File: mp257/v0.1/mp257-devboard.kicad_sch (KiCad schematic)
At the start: 39 parts, among them CON1 microSDCon_SMT_104031-0811, J1 Pins_02x40_P0.4mm_W3.0mm_SMT, J2 Pins_02x40_P0.4mm_W3.0mm_SMT, J3 USB-C_Receptacle_Molex_217179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, J4 Pins_02x04_RightAngle_P2.54mm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, J5 Conn_01x02, J6 Pins_02x05_P1.27mm_SMT, U1 STM32MP257FAK3, U3 USBLC6-2SC6, U5 NORFLASH_W25Q128JV, X1 XTAL_4_PINS

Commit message: Fix ref nums pasted from reference schematic
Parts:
- renumbered C4 to C90, C3 to C92, X1 to X2
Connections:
- net GND: now also S3.1; no longer R72.2
- net VDD: now also R72.2; no longer S3.1
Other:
- sheet Power ports: added WAKEUP_BUT; removed none
- note added: "NOR Flash"
- moved on the sheet: BOOT0_2, C21, J1, J2, J3, J5, R10, R11, R3, R4, R5, R6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

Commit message: Fix all refs: no duplicates
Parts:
- renumbered C12 to C120, C21 to C210, R11 to R12, R2 to R9
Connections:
- no-connect marks 198 -> 199
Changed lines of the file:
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@@
 	)
 	(no_connect
+		(at 189.23 481.33)
+	)
+	(no_connect
 		(at 346.71 518.16)
 	)
@@
 		(dnp no)
 		(fields_autoplaced yes)
-		(property "Reference" "R2"
+		(property "Reference" "R9"
 			(at 175.26 275.5899 0)
 			(effects
@@
 			(project "mp153-devboard"
 				(path "/64ec1a6b-f4f9-4414-abbd-a05816451f08"
-					(reference "R2")
+					(reference "R9")
 					(unit 1)
 				)
@@
 		(dnp no)
 		(fields_autoplaced yes)
-		(property "Reference" "C21"
+		(property "Reference" "C210"
 			(at 231.14 202.5586 0)
 			(effects
@@
 			(project "Kit-Brainboard"
 				(path "/64ec1a6b-f4f9-4414-abbd-a05816451f08"
-					(reference "C21")
+					(reference "C210")
 					(unit 1)
 				)
@@
 		(dnp no)
 		(fields_autoplaced yes)
-		(property "Reference" "R11"
+		(property "Reference" "R12"
 			(at 279.4 88.8999 0)
 			(effects
@@
 			(project "mp153-devboard"
 				(path "/64ec1a6b-f4f9-4414-abbd-a05816451f08"
-					(reference "R11")
+					(reference "R12")
 					(unit 1)
 				)
@@
 		(dnp no)
 		(fields_autoplaced yes)
-		(property "Reference" "C12"
-			(at 102.87 268.6113 0)
+		(property "Reference" "C120"
+			(at 102.87 267.9762 0)
 			(effects
 				(font
@@
 		)
 		(property "Display" "0.1uF"
-			(at 102.87 271.1513 0)
+			(at 102.87 270.5162 0)
 			(effects
 				(font
@@
 			(project "Kit-Brainboard"
 				(path "/64ec1a6b-f4f9-4414-abbd-a05816451f08"
-					(reference "C12")
+					(reference "C120")
 					(unit 1)
 				)

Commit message: WIP: symbols
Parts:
- U1: symbol MCD_PARTS_database:U_STM32MP25XXAK I_Os_0_STM32MP257FAK3_MCD_PARTS_database.DbLib -> 4ms_IC:STM32MP257FAKx
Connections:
- net VDDA1V8_AON is gone; now on net VDDA_1V8: U1.W2 (PDR_ON)
- net PC10: no longer CON1.1 (DAT2), J1.13 (Pin_13), J1.14 (Pin_14)
- net PC11: no longer CON1.2 (CD/DAT3), J1.15 (Pin_15), J1.16 (Pin_16)
- net PC12: no longer CON1.5 (CLK), J1.19 (Pin_19), J1.20 (Pin_20)
- net PC8: no longer CON1.7 (DAT0), J1.7 (Pin_7), J1.8 (Pin_8), R1.2
- net PC9: no longer CON1.8 (DAT1), J1.10 (Pin_10), J1.9 (Pin_9)
- net PD2: no longer CON1.3 (CMD), J1.17 (Pin_17), J1.18 (Pin_18), R9.2
- net VDDIO renamed VDD_IO
- net eMMC.SDMMC2_CK: no longer names the net of U1.B25 (PE14)
- net eMMC.SDMMC2_CMD: no longer names the net of U1.D24 (PE15)
- net eMMC.SDMMC2_D0: no longer names the net of U1.C24 (PE13)
- net eMMC.SDMMC2_D1: no longer names the net of U1.B23 (PE11)
- net eMMC.SDMMC2_D2: no longer names the net of U1.C23 (PE8)
- net eMMC.SDMMC2_D3: no longer names the net of U1.C25 (PE12)
- net eMMC.SDMMC2_D4: no longer names the net of U1.D22 (PE10)
- net eMMC.SDMMC2_D5: no longer names the net of U1.A23 (PE9)
- net eMMC.SDMMC2_D6: no longer names the net of U1.A22 (PE6)
- net eMMC.SDMMC2_D7: no longer names the net of U1.B22 (PE7)
- new net SDMMC_CLK: CON1.5 (CLK), J1.19 (Pin_19), J1.20 (Pin_20)
- new net SDMMC_CMD: CON1.3 (CMD), J1.17 (Pin_17), J1.18 (Pin_18), R9.2
- new net SDMMC_D0: CON1.7 (DAT0), J1.7 (Pin_7), J1.8 (Pin_8), R1.2
- new net SDMMC_D1: CON1.8 (DAT1), J1.10 (Pin_10), J1.9 (Pin_9)
- new net SDMMC_D2: CON1.1 (DAT2), J1.13 (Pin_13), J1.14 (Pin_14)
- new net SDMMC_D3: CON1.2 (CD/DAT3), J1.15 (Pin_15), J1.16 (Pin_16)
- no-connect marks 199 -> 209
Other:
- note removed: "PMIC"

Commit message: Updated RAM and STM32MP2 footprints to 4ms lib
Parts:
- U1: footprint ICC_TFBGA424_14X14_P050_H1P20_CODE-B0A2 -> 4ms_Package_QFP:TFBGA-424_14x14mm_P0.5_STM_AK

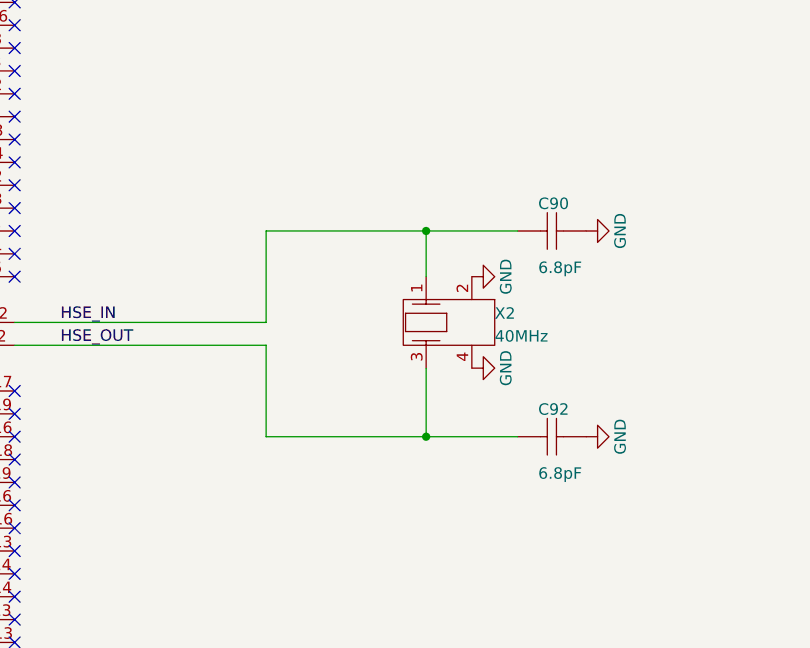
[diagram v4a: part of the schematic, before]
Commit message: Updating parts to 4ms lib
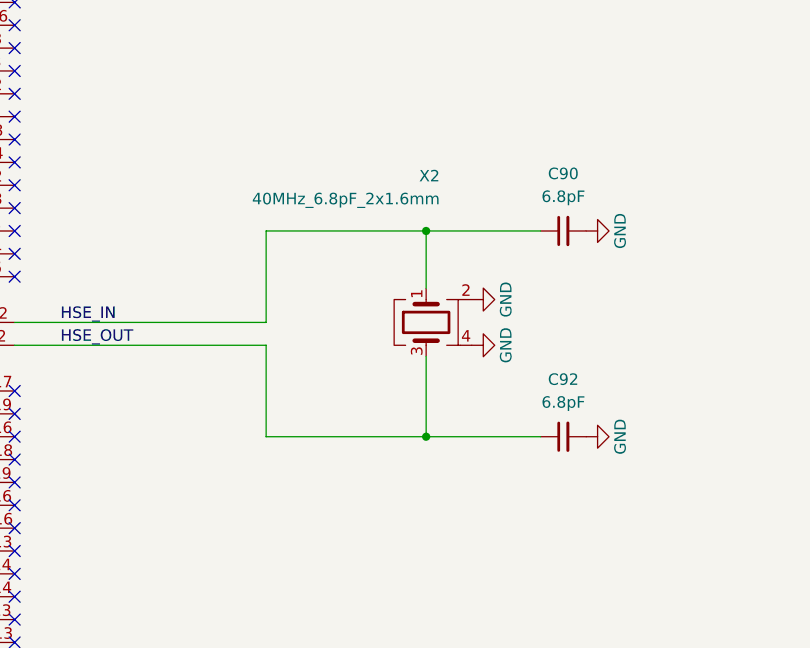
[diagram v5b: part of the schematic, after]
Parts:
- C90: value Capacitor -> 6.8pF_0402_25V; footprint C0402 -> 4ms_Capacitor:C_0402; symbol MCD_PARTS_database:U_STM32MP25XXAK I_Os_0_mirrored_Capacitor_MCD_PARTS_database.DbLib -> 4ms_Capacitor:6.8pF_0402_25V; ALTERNATE_MANUFACTURER N/A -> (none); ALTERNATE_MANUFACTURER_PART_NUMBER N/A -> (none); ALTIUM_VALUE 6.8pF -> (none); COMPONENTLINK1DESCRIPTION Datasheet -> (none); COMPONENTLINK1URL http://tunmcdsvn.tun.st.com/Component_Documentation_Library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 -> (none); COMPONENT_COUNTRY_OF_ORIGIN China -> (none); Display (none) -> 6.8pF; ECCN_EU n/a -> (none); ECCN_US n/a -> (none); ID 3068 -> (none); INITIAL_BOARD_REFERENCE MB1319 -> (none); INTERNAL_PART_NUMBER MCD-00674 -> (none); JLCPCB ID (none) -> C1576; MANUFACTURER YAGEO -> (none); MANUFACTURER_PART_NUMBER CC0402CRNPO9BN6R8 -> (none); Manufacturer (none) -> Yageo; ORDER_CODE_DIGIKEY 311-3327-1-ND -> (none); ORDER_CODE_FARNELL N/A -> (none); ORDER_CODE_RS N/A -> (none); PACKAGE 0402 -> (none); PART_PREFERENCE Recommended -> (none); PART_TYPE Capacitor -> (none); PROVIDED_BY SUBCO -> (none); Part Number (none) -> CC0402CRNPO9BN6R8; Production Stage (none) -> A; SHOWFIELDS YES -> (none); STATUS Released -> (none); Specifications (none) -> 6.8pF, Min. 25V 10%, NP0/C0G
- C92: value Capacitor -> 6.8pF_0402_25V; footprint C0402 -> 4ms_Capacitor:C_0402; symbol MCD_PARTS_database:U_STM32MP25XXAK I_Os_2_mirrored_Capacitor_MCD_PARTS_database.DbLib -> 4ms_Capacitor:6.8pF_0402_25V; ALTERNATE_MANUFACTURER N/A -> (none); ALTERNATE_MANUFACTURER_PART_NUMBER N/A -> (none); ALTIUM_VALUE 6.8pF -> (none); COMPONENTLINK1DESCRIPTION Datasheet -> (none); COMPONENTLINK1URL http://tunmcdsvn.tun.st.com/Component_Documentation_Library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 -> (none); COMPONENT_COUNTRY_OF_ORIGIN China -> (none); Display (none) -> 6.8pF; ECCN_EU n/a -> (none); ECCN_US n/a -> (none); ID 3068 -> (none); INITIAL_BOARD_REFERENCE MB1319 -> (none); INTERNAL_PART_NUMBER MCD-00674 -> (none); JLCPCB ID (none) -> C1576; MANUFACTURER YAGEO -> (none); MANUFACTURER_PART_NUMBER CC0402CRNPO9BN6R8 -> (none); Manufacturer (none) -> Yageo; ORDER_CODE_DIGIKEY 311-3327-1-ND -> (none); ORDER_CODE_FARNELL N/A -> (none); ORDER_CODE_RS N/A -> (none); PACKAGE 0402 -> (none); PART_PREFERENCE Recommended -> (none); PART_TYPE Capacitor -> (none); PROVIDED_BY SUBCO -> (none); Part Number (none) -> CC0402CRNPO9BN6R8; Production Stage (none) -> A; SHOWFIELDS YES -> (none); STATUS Released -> (none); Specifications (none) -> 6.8pF, Min. 25V 10%, NP0/C0G
- X2: value XTAL_4_PINS -> 40MHz_6.8pF_2x1.6mm; footprint CRY_NX1612SA_4P -> 4ms_Crystal:Crystal_2.0x1.6mm_4pin; symbol MCD_PARTS_database:U_STM32MP25XXAK I_Os_0_XTAL_4_PINS_MCD_PARTS_database.DbLib -> 4ms_Crystal:40MHz_6.8pF_2x1.6mm; ALTIUM_VALUE 40MHz -> (none); COMPONENTLINK1URL http://tunmcdsvn.tun.st.com/Component_Documentation_Library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 -> (none); COMPONENT_COUNTRY_OF_ORIGIN Unknown -> (none); ID 4450 -> (none); INTERNAL_PART_NUMBER MCD-02344 -> (none); MANUFACTURER NDK -> (none); MANUFACTURER_PART_NUMBER NX1612SA-40MHZ-EXS00A-CS13836 -> (none); Manufacturer (none) -> ECS; ORDER_CODE_DIGIKEY N/A -> (none); ORDER_CODE_FARNELL N/A -> (none); ORDER_CODE_RS N/A -> (none); PACKAGE 1.6x1.2mm -> (none); PART_PREFERENCE Recommended -> (none); PART_TYPE Crystal_Osc -> (none); Production Stage (none) -> A; SHOWFIELDS YES -> (none); STATUS Checked -> (none); Specifications (none) -> 40MHz 6.8pF Crystal Resonator, 10ppm, 2016 2x1.6mm
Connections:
- net GND: now also C90.2; no longer C90.1
- net HSE_IN: now also C90.1; no longer C90.2
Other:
- moved on the sheet: X2

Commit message: WIP
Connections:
- net NRSTC1MS: now also R272.1; no longer R272.2
- net PWR_CPU_ON: now also R272.2; no longer R272.1
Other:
- moved on the sheet: R272
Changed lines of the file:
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@@
 	(symbol
 		(lib_id "4ms_Resistor_0402:10k_0402")
-		(at 153.67 485.14 0)
+		(at 153.67 485.14 180)
 		(unit 1)
 		(exclude_from_sim no)
@@
 		(on_board yes)
 		(dnp no)
+		(fields_autoplaced yes)
 		(property "Reference" "R272"
-			(at 156.972 482.346 0)
+			(at 156.21 483.8699 0)
 			(effects
 				(font
 					(size 1.27 1.27)
 				)
-				(justify left bottom)
+				(justify right)
 			)
 		)
 		(property "Value" "10k_0402"
-			(at 151.13 485.14 90)
+			(at 156.21 485.14 90)
 			(effects
 				(font
@@
 		)
 		(property "Footprint" "4ms_Resistor:R_0402"
-			(at 151.13 498.094 0)
+			(at 156.21 472.186 0)
 			(effects
 				(font
@@
 		)
 		(property "Specifications" "10k, 1%, 1/16W, 0402"
-			(at 151.13 492.76 0)
+			(at 156.21 477.52 0)
 			(effects
 				(font
@@
 		)
 		(property "Manufacturer" "Yageo"
-			(at 151.13 494.538 0)
+			(at 156.21 475.742 0)
 			(effects
 				(font
@@
 		)
 		(property "Part Number" "RC0402FR-0710KL"
-			(at 151.13 496.316 0)
+			(at 156.21 473.964 0)
 			(effects
 				(font
@@
 		)
 		(property "Display" "10k"
-			(at 157.48 485.14 90)
+			(at 156.21 486.4099 0)
 			(effects
 				(font
 					(size 1.27 1.27)
 				)
+				(justify right)
 			)
 		)
 		(property "JLCPCB ID" "C60490"
-			(at 151.13 499.872 0)
+			(at 156.21 470.408 0)
 			(effects
 				(font
@@
 		)
 		(property "Production Stage" "A"
-			(at 151.13 501.65 0)
+			(at 156.21 468.63 0)
 			(effects
 				(font

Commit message: mp257 placement WIP
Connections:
- net PA0: no longer J2.31 (Pin_31), J2.32 (Pin_32)
- net PA1: no longer J2.33 (Pin_33), J2.34 (Pin_34)
- net PA2: no longer J2.35 (Pin_35), J2.36 (Pin_36)
- net PA3: no longer J2.53 (Pin_53), J2.54 (Pin_54)
- net PA4: no longer J2.41 (Pin_41), J2.42 (Pin_42)
- net PA5: no longer J2.37 (Pin_37), J2.38 (Pin_38)
- net PA6: no longer J2.57 (Pin_57), J2.58 (Pin_58)
- net PA7: no longer J2.29 (Pin_29), J2.30 (Pin_30)
- net PB1: no longer J2.47 (Pin_47), J2.48 (Pin_48)
- net PC1: no longer J2.49 (Pin_49), J2.50 (Pin_50)
- net PC2: no longer J2.61 (Pin_61), J2.62 (Pin_62)
- net PC3: no longer J2.55 (Pin_55), J2.56 (Pin_56)
- net PC4: no longer J2.43 (Pin_43), J2.44 (Pin_44)
- net PC5: no longer J2.45 (Pin_45), J2.46 (Pin_46)
- net PF11: no longer J2.39 (Pin_39), J2.40 (Pin_40)
- net PF12: no longer J2.59 (Pin_59), J2.60 (Pin_60)
- net PG13: no longer J2.51 (Pin_51), J2.52 (Pin_52)
- net ADC3_CH4: now reaches U1.AA13 (PH9)
- net ADC1_CH11: now reaches U1.AA15 (PF0)
- net ADC1_CH11: now also J2.55 (Pin_55), J2.56 (Pin_56)
- net ADC1_CH3: now reaches U1.AA7 (PG3)
- net ADC1_CH13: now reaches U1.AC15 (PF2)
- net ADC1_CH6: now reaches U1.AD4 (PG1)
- net ADC1_CH4: now reaches U1.AD6 (PG4)
- net ADC3_CH6: now reaches U1.AE4 (PF11)
- net ADC3_CH2: now reaches U1.AE5 (PF10)
- net ADC1_CH16: now reaches U1.AF11 (PF3)
- net ADC3_CH8: now reaches U1.AF14 (PH10)
- net ADC1_CH2: now reaches U1.AG5 (PG2)
- net ADC1_CH12: now reaches U1.AA9 (PC3)
- net ADC1_CH12: now also J2.59 (Pin_59), J2.60 (Pin_60)
- net ADC1_CH9: now reaches U1.AB10 (PC6)
- net ADC1_CH10: now reaches U1.AD10 (PC5)
- net ADC1_CH7: now reaches U1.AD8 (PC11)
- net ADC1_CH15: now reaches U1.AE6 (PB15)
- net ADC1_CH17: now reaches U1.AE7 (PC12)
- net ADC1_CH8: now reaches U1.AE9 (PC9)
- net ADC1_CH8: now also J2.57 (Pin_57), J2.58 (Pin_58)
- net ADC3_CH9: now reaches U1.AF9 (PC7)
- net ADC1_CH5: now reaches U1.AG10 (PC10)
- net ADC1_CH5: now also J2.53 (Pin_53), J2.54 (Pin_54)
- new net: J2.29 (Pin_29), J2.30 (Pin_30)
- new net: J2.31 (Pin_31), J2.32 (Pin_32)
- new net: J2.33 (Pin_33), J2.34 (Pin_34)
- new net: J2.35 (Pin_35), J2.36 (Pin_36)
- new net: J2.37 (Pin_37), J2.38 (Pin_38)
- new net: J2.39 (Pin_39), J2.40 (Pin_40)
- new net: J2.41 (Pin_41), J2.42 (Pin_42)
- new net: J2.43 (Pin_43), J2.44 (Pin_44)
- new net: J2.45 (Pin_45), J2.46 (Pin_46)
- new net: J2.47 (Pin_47), J2.48 (Pin_48)
- new net: J2.49 (Pin_49), J2.50 (Pin_50)
- new net: J2.51 (Pin_51), J2.52 (Pin_52)
- new net: J2.61 (Pin_61), J2.62 (Pin_62)
- no-connect marks 209 -> 89
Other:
- note added: "SPI-MISO"
- note added: "SPI-MOSI"
- note added: "SPI-NSS"
- note added: "SPI-SCK"
- note added: "SPI3"
- note added: "SPI5"
- note removed: "ADC2-6"
- note removed: "SPI1-MISO"
- note removed: "SPI1-MOSI"
- note removed: "SPI1-NSS"
- note removed: "SPI1-SCK"

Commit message: Routing SDMMC, SAI, I2C, ADCs
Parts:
- added J7: Conn_02x15_Odd_Even, 4ms_Connector:Connector-30pin-P0.4mm-W3.0mm, symbol Connector_Generic:Conn_02x15_Odd_Even
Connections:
- net ADC1_CH3: now also J2.17 (Pin_17), J2.18 (Pin_18)
- net ADC1_CH6: now also J2.37 (Pin_37), J2.38 (Pin_38)
- net ADC1_CH9: now also J2.73 (Pin_73), J2.74 (Pin_74)
- net ADC3_CH8: now also J2.61 (Pin_61), J2.62 (Pin_62)
- net BOOT0: now also U1.Y3 (BOOT0)
- net BOOT2: now also U1.AB1 (BOOT2)
- net GND: now also J7.1 (Pin_1), J7.3 (Pin_3), J7.5 (Pin_5), J7.7 (Pin_7), J7.9 (Pin_9)
- net PA10: no longer J1.63 (Pin_63), J1.64 (Pin_64)
- net PA11: no longer J1.55 (Pin_55), J1.56 (Pin_56)
- net PA5: now also J2.75 (Pin_75), J2.76 (Pin_76), U1.AE17 (PA5)
- net PA9: now also J2.71 (Pin_71), J2.72 (Pin_72), U1.AF15 (PA9); no longer J2.5 (Pin_5), J2.6 (Pin_6)
- net PB14: no longer J1.39 (Pin_39), J1.40 (Pin_40)
- net PB15: no longer J1.5 (Pin_5), J1.6 (Pin_6)
- net PB4: no longer J1.1 (Pin_1), J1.2 (Pin_2)
- net PB6: now also J1.3 (Pin_3), J1.4 (Pin_4), U1.C13 (PB6); no longer J2.13 (Pin_13), J2.14 (Pin_14)
- net PB8: no longer J1.3 (Pin_3), J1.4 (Pin_4)
- net PB9: no longer CON1.10 (SDDET1), J1.11 (Pin_11), J1.12 (Pin_12)
- net PD0: no longer J1.43 (Pin_43), J1.44 (Pin_44)
- net PD12: no longer J1.61 (Pin_61), J1.62 (Pin_62)
- net PD14: no longer J2.3 (Pin_3), J2.4 (Pin_4)
- net PD3: no longer J1.41 (Pin_41), J1.42 (Pin_42)
- net PD6: no longer J1.49 (Pin_49), J1.50 (Pin_50)
- net PD7: no longer J2.71 (Pin_71), J2.72 (Pin_72)
- net PE11: no longer J1.45 (Pin_45), J1.46 (Pin_46)
- net PE12: no longer J2.1 (Pin_1), J2.2 (Pin_2)
- net PE13: no longer J2.17 (Pin_17), J2.18 (Pin_18)
- net PE5: no longer J1.57 (Pin_57), J1.58 (Pin_58)
- net PE8: no longer J1.59 (Pin_59), J1.60 (Pin_60)
- net PF1: no longer J2.15 (Pin_15), J2.16 (Pin_16)
- net PF3: no longer J2.11 (Pin_11), J2.12 (Pin_12)
- net PG10: no longer J1.51 (Pin_51), J1.52 (Pin_52)
- net PG12: no longer J2.75 (Pin_75), J2.76 (Pin_76)
- net PG2: no longer J2.69 (Pin_69), J2.70 (Pin_70)
- net PG7: no longer J2.21 (Pin_21), J2.22 (Pin_22)
- net PH12: no longer J1.47 (Pin_47), J1.48 (Pin_48)
- net PH13: no longer J2.19 (Pin_19), J2.20 (Pin_20)
- net PH14: no longer J2.7 (Pin_7), J2.8 (Pin_8)
- net PH3: no longer J2.73 (Pin_73), J2.74 (Pin_74)
- net PH8: no longer J2.10 (Pin_10), J2.9 (Pin_9)
- net SDMMC_CLK: now also U1.C21 (PE3)
- net SDMMC_CMD: now also U1.C20 (PE2)
- net SDMMC_D0: now also U1.B21 (PE4)
- net SDMMC_D1: now also U1.C22 (PE5)
- net SDMMC_D2: now also U1.B19 (PE0)
- net SDMMC_D3: now also U1.C19 (PE1)
- net LTDC_VSYNC: now reaches U1.J3 (PI6)
- net LTDC_VSYNC: now also J7.2 (Pin_2)
- net LTDC_HSYNC: now reaches U1.J5 (PI7)
- net LTDC_HSYNC: now also J7.12 (Pin_12)
- net LTDC_DE: now reaches U1.K4 (PI5)
- net LTDC_DE: now also J7.4 (Pin_4)
- net LTDC_B3: now reaches U1.L7 (PI0)
- net LTDC_B3: now also J7.23 (Pin_23)
- net LTDC_B4: now reaches U1.M6 (PI1)
- net LTDC_B4: now also J7.21 (Pin_21)
- net LTDC_B5: now reaches U1.N5 (PI2)
- net LTDC_B5: now also J7.10 (Pin_10)
- net LTDC_B6: now reaches U1.N7 (PI3)
- net LTDC_B6: now also J7.8 (Pin_8)
- net LTDC_B7: now reaches U1.P6 (PI4)
- net LTDC_B7: now also J7.6 (Pin_6)
- net PE9: now reaches U1.A23 (PE9)
- net PE9: now also J1.41 (Pin_41), J1.42 (Pin_42)
- net PH7: now reaches U1.AE16 (PH7)
- net PH7: now also J2.5 (Pin_5), J2.6 (Pin_6)
- net PF9: now reaches U1.AE8 (PF9)
- net PF9: now also J2.1 (Pin_1), J2.2 (Pin_2)
- net SAI1_FS: now reaches U1.B23 (PE11)
- net SAI1_FS: now also J1.45 (Pin_45), J1.46 (Pin_46)
- net SAI1_MCLK: now reaches U1.B25 (PE14)
- net SAI1_MCLK: now also J1.43 (Pin_43), J1.44 (Pin_44)
- net SAI1_SD_A: now reaches U1.C24 (PE13)
- net SAI1_SD_A: now also J1.49 (Pin_49), J1.50 (Pin_50)
- net SAI1_SCK: now reaches U1.D24 (PE15)
- net SAI1_SCK: now also J1.47 (Pin_47), J1.48 (Pin_48)
- net LTDC_G2: now reaches U1.L5 (PG8)
- net LTDC_G2: now also J7.20 (Pin_20)
- net LTDC_G3: now reaches U1.M3 (PG9)
- net LTDC_G3: now also J7.22 (Pin_22)
- net LTDC_G4: now reaches U1.M4 (PG10)
- net LTDC_G4: now also J7.24 (Pin_24)
- net LTDC_G5: now reaches U1.N2 (PG11)
- net LTDC_G5: now also J7.26 (Pin_26)
- net LTDC_G6: now reaches U1.N3 (PG12)
- net LTDC_G6: now also J7.28 (Pin_28)
- net LTDC_G7: now reaches U1.P1 (PG13)
- net LTDC_G7: now also J7.30 (Pin_30)
- net LTDC_R3: now reaches U1.P3 (PF14)
- net LTDC_R3: now also J7.27 (Pin_27)
- net LTDC_CLK: now reaches U1.P4 (PF12)
- net LTDC_CLK: now also J7.25 (Pin_25)
- net LTDC_R4: now reaches U1.R2 (PF15)
- net LTDC_R4: now also J7.29 (Pin_29)
- net LTDC_R5: now reaches U1.R3 (PG5)
- net LTDC_R5: now also J7.14 (Pin_14)
- net LTDC_R6: now reaches U1.T3 (PG6)
- net LTDC_R6: now also J7.16 (Pin_16)
- net LTDC_R7: now reaches U1.U2 (PG7)
- net LTDC_R7: now also J7.18 (Pin_18)
- net I2C4_SCL: now reaches U1.A15 (PD11)
- net I2C4_SCL: now also J1.61 (Pin_61), J1.62 (Pin_62)
- net SAI1_SD_B: now reaches U1.A26 (PB13)
- net SAI1_SD_B: now also J1.51 (Pin_51), J1.52 (Pin_52)
- net I2C4_SDA: now reaches U1.C17 (PD10)
- net I2C4_SDA: now also J1.59 (Pin_59), J1.60 (Pin_60)
- new net: J2.10 (Pin_10), J2.9 (Pin_9)
- new net: J2.11 (Pin_11), J2.12 (Pin_12)
- new net: J2.13 (Pin_13), J2.14 (Pin_14)
- new net: J2.15 (Pin_15), J2.16 (Pin_16)
- new net: J2.19 (Pin_19), J2.20 (Pin_20)
- new net: J2.21 (Pin_21), J2.22 (Pin_22)
- new net: J2.3 (Pin_3), J2.4 (Pin_4)
- new net: J2.69 (Pin_69), J2.70 (Pin_70)
- new net: J2.7 (Pin_7), J2.8 (Pin_8)
- new net: J1.1 (Pin_1), J1.2 (Pin_2)
- new net: J1.11 (Pin_11), J1.12 (Pin_12)
- new net: J1.39 (Pin_39), J1.40 (Pin_40)
- new net: J1.5 (Pin_5), J1.6 (Pin_6)
- new net: J1.55 (Pin_55), J1.56 (Pin_56)
- new net: J1.57 (Pin_57), J1.58 (Pin_58)
- new net: J1.63 (Pin_63), J1.64 (Pin_64)
- no-connect marks 89 -> 77
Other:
- note added: "I2C4_SCL"
- note added: "I2C4_SDA"
- note added: "SAI2_FS_B"
- note added: "SAI2_SCK_B"
- note added: "SAI2_SD_A"
- note added: "SAI2_SD_B"
- note added: "UART4_RX"
- note added: "UART4_TX"
- note removed: "SDMMC_CLK"
- note removed: "SDMMC_D0"
- note removed: "SDMMC_D1"
- note removed: "SDMMC_D2"
- note removed: "SDMMC_D3"
- note removed: "SPI5"
- moved on the sheet: J3, J5, R10, R12, R3, R4, R5, R6, R7, R8, U3
